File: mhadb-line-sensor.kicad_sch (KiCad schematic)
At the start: 112 parts, among them J1 TC2030, J2 Conn_01x04_Pin, J3 Conn_01x04, J4 Conn_01x04_Pin, SW1 SW_Push, SW2 SW_Push, SW3 SW_Push, SW4 SW_Push, U1 HT753-1, U10 QRE1113GR, U11 QRE1113GR, U12 QRE1113GR, U13 QRE1113GR, U2 SN65HVD230, U3 STM32F103C8Tx, U4 QRE1113GR, U5 QRE1113GR, U6 QRE1113GR, U7 QRE1113GR, U8 QRE1113GR, U9 QRE1113GR, Y1 8M

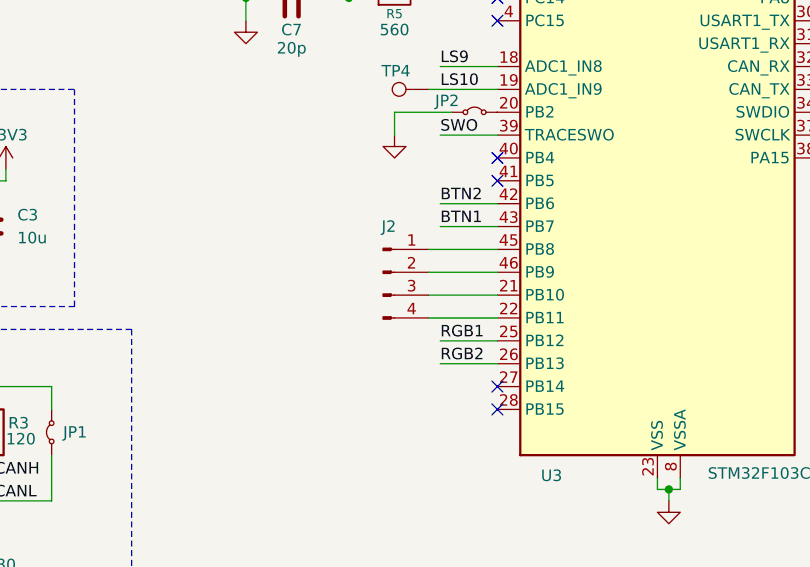
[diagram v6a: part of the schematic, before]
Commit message: schem/pcb: remove spare GPIOs
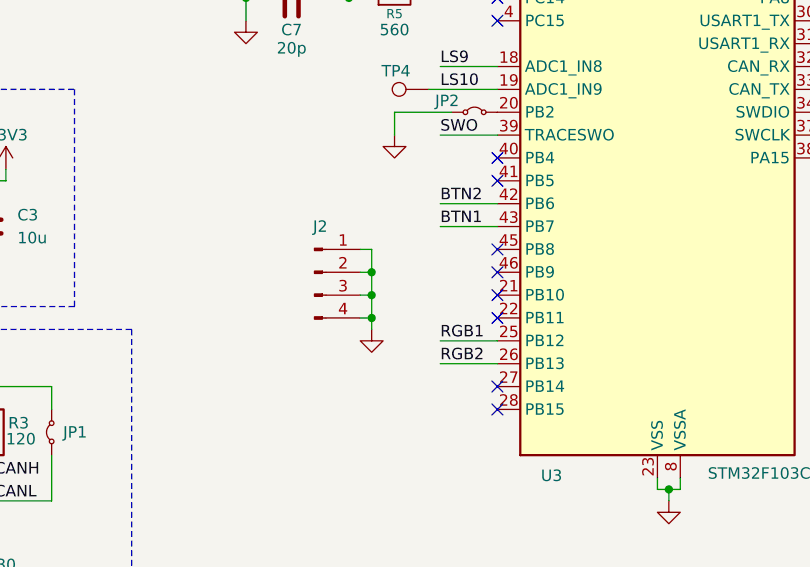
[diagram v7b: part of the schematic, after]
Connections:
- net GND: now also J2.1 (Pin_1), J2.2 (Pin_2), J2.3 (Pin_3), J2.4 (Pin_4)
- net at U3.21 (PB10): no longer J2.3 (Pin_3)
- net at U3.22 (PB11): no longer J2.4 (Pin_4)
- net at U3.45 (PB8): no longer J2.1 (Pin_1)
- net at U3.46 (PB9): no longer J2.2 (Pin_2)
- no-connect marks 11 -> 15
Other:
- moved on the sheet: J2
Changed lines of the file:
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@@
 	)
 	(junction
+		(at 93.98 118.11)
+		(diameter 0)
+		(color 0 0 0 0)
+	)
+	(junction
 		(at 234.95 25.4)
 		(diameter 0)
@@
 	)
 	(junction
+		(at 93.98 115.57)
+		(diameter 0)
+		(color 0 0 0 0)
+	)
+	(junction
 		(at 49.53 190.5)
 		(diameter 0)
@@
 	)
 	(junction
+		(at 93.98 120.65)
+		(diameter 0)
+		(color 0 0 0 0)
+	)
+	(junction
 		(at 208.28 58.42)
 		(diameter 0)
@@
 	)
 	(no_connect
+		(at 107.95 118.11)
+	)
+	(no_connect
 		(at 276.86 130.81)
 	)
@@
 	)
 	(no_connect
+		(at 107.95 115.57)
+	)
+	(no_connect
 		(at 107.95 82.55)
 	)
@@
 		(at 107.95 128.27)
 	)
+	(no_connect
+		(at 107.95 113.03)
+	)
+	(no_connect
+		(at 107.95 120.65)
+	)
 	(wire
 		(pts
@@
 	(wire
 		(pts
-			(xy 107.95 120.65) (xy 100.33 120.65)
-		)
-		(stroke
-			(width 0)
-			(type default)
-		)
-	)
-	(wire
-		(pts
 			(xy 252.73 139.7) (xy 269.24 139.7)
 		)
@@
 	(wire
 		(pts
+			(xy 93.98 120.65) (xy 93.98 118.11)
+		)
+		(stroke
+			(width 0)
+			(type default)
+		)
+	)
+	(wire
+		(pts
 			(xy 245.11 53.34) (xy 243.84 53.34)
 		)
@@
 	(wire
 		(pts
-			(xy 107.95 113.03) (xy 100.33 113.03)
-		)
-		(stroke
-			(width 0)
-			(type default)
-		)
-	)
-	(wire
-		(pts
 			(xy 243.84 25.4) (xy 245.11 25.4)
 		)
@@
 	(wire
 		(pts
+			(xy 93.98 118.11) (xy 92.71 118.11)
+		)
+		(stroke
+			(width 0)
+			(type default)
+		)
+	)
+	(wire
+		(pts
 			(xy 226.06 58.42) (xy 226.06 59.69)
 		)
@@
 	(wire
 		(pts
-			(xy 107.95 115.57) (xy 100.33 115.57)
-		)
-		(stroke
-			(width 0)
-			(type default)
-		)
-	)
-	(wire
-		(pts
 			(xy 166.37 69.85) (xy 166.37 90.17)
 		)
@@
 	(wire
 		(pts
+			(xy 93.98 115.57) (xy 92.71 115.57)
+		)
+		(stroke
+			(width 0)
+			(type default)
+		)
+	)
+	(wire
+		(pts
 			(xy 138.43 34.29) (xy 139.7 34.29)
 		)
@@
 	(wire
 		(pts
+			(xy 93.98 120.65) (xy 92.71 120.65)
+		)
+		(stroke
+			(width 0)
+			(type default)
+		)
+	)
+	(wire
+		(pts
 			(xy 118.11 53.34) (xy 118.11 52.07)
 		)
@@
 	(wire
 		(pts
+			(xy 93.98 121.92) (xy 93.98 120.65)
+		)
+		(stroke
+			(width 0)
+			(type default)
+		)
+	)
+	(wire
+		(pts
 			(xy 39.37 113.03) (xy 39.37 115.57)
 		)
@@
 	(wire
 		(pts
+			(xy 93.98 115.57) (xy 93.98 113.03)
+		)
+		(stroke
+			(width 0)
+			(type default)
+		)
+	)
+	(wire
+		(pts
 			(xy 132.08 180.34) (xy 138.43 180.34)
 		)
@@
 	(wire
 		(pts
+			(xy 93.98 118.11) (xy 93.98 115.57)
+		)
+		(stroke
+			(width 0)
+			(type default)
+		)
+	)
+	(wire
+		(pts
 			(xy 36.83 189.23) (xy 36.83 190.5)
 		)
@@
 	(wire
 		(pts
-			(xy 107.95 118.11) (xy 100.33 118.11)
-		)
-		(stroke
-			(width 0)
-			(type default)
-		)
-	)
-	(wire
-		(pts
 			(xy 24.13 62.23) (xy 29.21 62.23)
 		)
@@
 	(wire
 		(pts
+			(xy 93.98 113.03) (xy 92.71 113.03)
+		)
+		(stroke
+			(width 0)
+			(type default)
+		)
+	)
+	(wire
+		(pts
 			(xy 30.48 27.94) (xy 30.48 29.21)
 		)
@@
 	(symbol
 		(lib_id "power:GND")
+		(at 93.98 121.92 0)
+		(unit 1)
+		(exclude_from_sim no)
+		(in_bom yes)
+		(on_board yes)
+		(dnp no)
+		(fields_autoplaced yes)
+		(property "Reference" "#PWR063"
+			(at 93.98 128.27 0)
+			(effects
+				(font
+					(size 1.27 1.27)
+				)
+				(hide yes)
+			)
+		)
+		(property "Value" "GND"
+			(at 93.98 127 0)
+			(effects
+				(font
+					(size 1.27 1.27)
+				)
+				(hide yes)
+			)
+		)
+		(property "Footprint" ""
+			(at 93.98 121.92 0)
+			(effects
+				(font
+					(size 1.27 1.27)
+				)
+				(hide yes)
+			)
+		)
+		(property "Datasheet" ""
+			(at 93.98 121.92 0)
+			(effects
+				(font
+					(size 1.27 1.27)
+				)
+				(hide yes)
+			)
+		)
+		(property "Description" "Power symbol creates a global label with name \"GND\" , ground"
+			(at 93.98 121.92 0)
+			(effects
+				(font
+					(size 1.27 1.27)
+				)
+				(hide yes)
+			)
+		)
+		(pin "1"
+		)
+		(instances
+			(project "mhadb-line-sensor"
+				(path "/dc023b14-f8af-47bb-9afb-84a8ab4a9288"
+					(reference "#PWR063")
+					(unit 1)
+				)
+			)
+		)
+	)
+	(symbol
+		(lib_id "power:GND")
 		(at 77.47 54.61 0)
 		(unit 1)
@@
 	(symbol
 		(lib_id "Connector:Conn_01x04_Pin")
-		(at 95.25 115.57 0)
+		(at 87.63 115.57 0)
 		(unit 1)
 		(exclude_from_sim no)
@@
 		(fields_autoplaced yes)
 		(property "Reference" "J2"
-			(at 95.885 110.49 0)
+			(at 88.265 110.49 0)
 			(effects
 				(font
@@
 		)
 		(property "Value" "Conn_01x04_Pin"
-			(at 92.71 116.84 90)
+			(at 85.09 116.84 90)
 			(effects
 				(font
@@
 		)
 		(property "Footprint" "Connector_PinHeader_2.54mm:PinHeader_1x04_P2.54mm_Vertical"
-			(at 95.25 115.57 0)
+			(at 87.63 115.57 0)
 			(effects
 				(font
@@
 		)
 		(property "Datasheet" "~"
-			(at 95.25 115.57 0)
+			(at 87.63 115.57 0)
 			(effects
 				(font
@@
 		)
 		(property "Description" "Generic connector, single row, 01x04, script generated"
-			(at 95.25 115.57 0)
+			(at 87.63 115.57 0)
 			(effects
 				(font

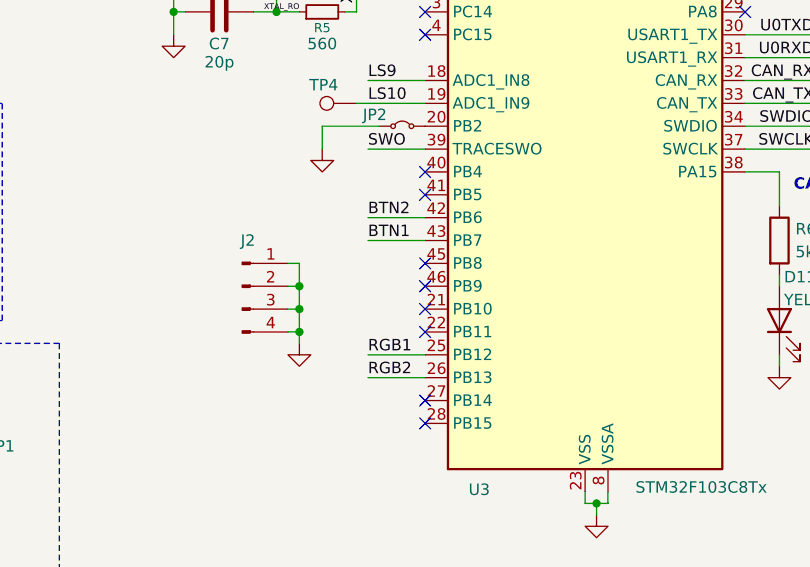
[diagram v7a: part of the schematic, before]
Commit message: pcb: add stitching vias
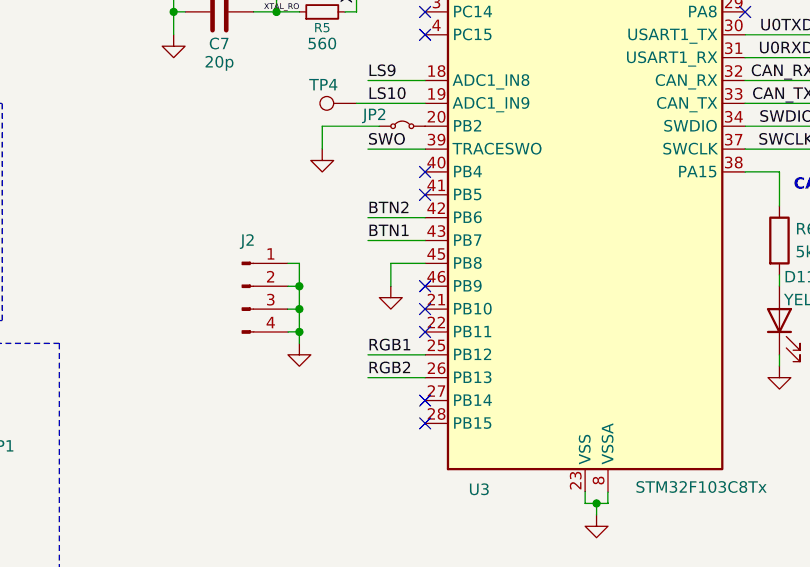
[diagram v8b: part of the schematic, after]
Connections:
- net GND: now also U3.45 (PB8)
- no-connect marks 15 -> 14
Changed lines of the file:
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@@
 	)
 	(no_connect
-		(at 107.95 113.03)
-	)
-	(no_connect
 		(at 107.95 120.65)
 	)
@@
 	(wire
 		(pts
+			(xy 104.14 113.03) (xy 104.14 115.57)
+		)
+		(stroke
+			(width 0)
+			(type default)
+		)
+	)
+	(wire
+		(pts
 			(xy 118.11 43.18) (xy 118.11 44.45)
 		)
@@
 	(wire
 		(pts
+			(xy 107.95 113.03) (xy 104.14 113.03)
+		)
+		(stroke
+			(width 0)
+			(type default)
+		)
+	)
+	(wire
+		(pts
 			(xy 219.71 118.11) (xy 219.71 119.38)
 		)
@@
 					(unit 1)
 				)
+			)
+		)
+	)
+	(symbol
+		(lib_id "power:GND")
+		(at 104.14 115.57 0)
+		(unit 1)
+		(exclude_from_sim no)
+		(in_bom yes)
+		(on_board yes)
+		(dnp no)
+		(fields_autoplaced yes)
+		(property "Reference" "#PWR064"
+			(at 104.14 121.92 0)
+			(effects
+				(font
+					(size 1.27 1.27)
+				)
+				(hide yes)
+			)
+		)
+		(property "Value" "GND"
+			(at 104.14 120.65 0)
+			(effects
+				(font
+					(size 1.27 1.27)
+				)
+				(hide yes)
+			)
+		)
+		(property "Footprint" ""
+			(at 104.14 115.57 0)
+			(effects
+				(font
+					(size 1.27 1.27)
+				)
+				(hide yes)
+			)
+		)
+		(property "Datasheet" ""
+			(at 104.14 115.57 0)
+			(effects
+				(font
+					(size 1.27 1.27)
+				)
+				(hide yes)
+			)
+		)
+		(property "Description" "Power symbol creates a global label with name \"GND\" , ground"
+			(at 104.14 115.57 0)
+			(effects
+				(font
+					(size 1.27 1.27)
+				)
+				(hide yes)
+			)
+		)
+		(pin "1"
+		)
+		(instances
+			(project "mhadb-line-sensor"
+				(path "/dc023b14-f8af-47bb-9afb-84a8ab4a9288"
+					(reference "#PWR064")
+					(unit 1)
+				)
